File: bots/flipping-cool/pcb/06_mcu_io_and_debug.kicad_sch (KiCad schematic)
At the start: 12 parts, among them J12 UART_PROGRAM_HEADER, J13 USB_C_GCT_USB4085, J44 DEBUG_UART_TX_RX, J46 DEBUG_EN_BOOT, J47 DEBUG_MODE_SENSE, J48 DEBUG_ADC, J49 STEMMA_QT_I2C, U10 ESP32-S3-WROOM-1, U11 USBLC6-2SC6

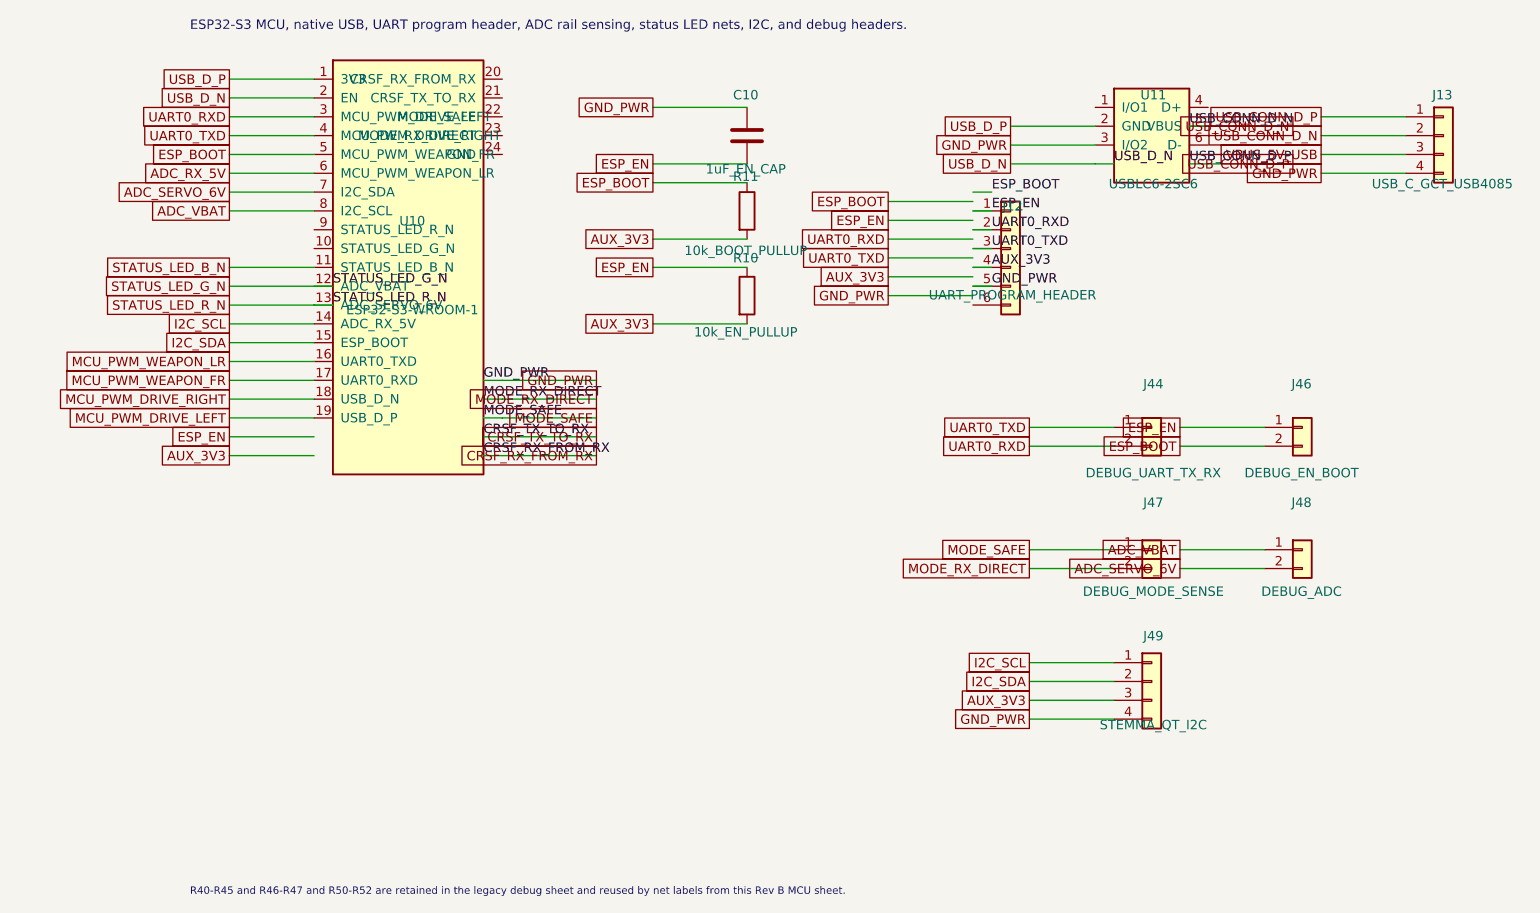
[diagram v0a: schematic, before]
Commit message: Remove obsolete Flipping Cool Rev B project plan file and update schematic files to reflect the latest design changes, including integration of the ESP32-S3 module and enhancements to power management and control authority. Ensure all documentation is aligned with the current PCB design and architecture.
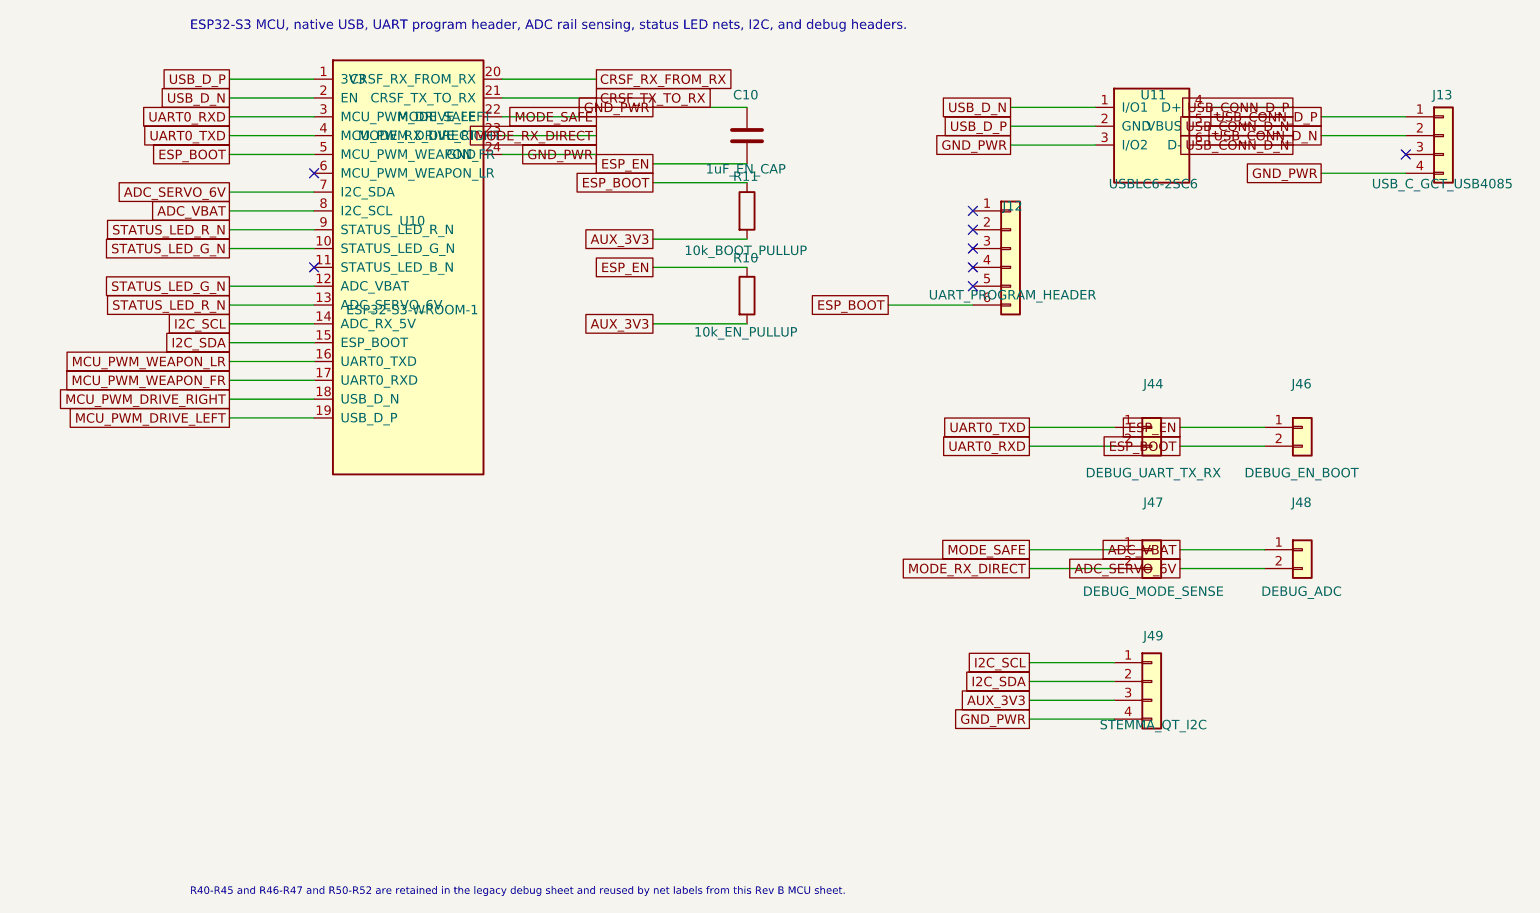
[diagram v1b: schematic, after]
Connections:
- net AUX_3V3: no longer J12.4 (Pin_4)
- net CRSF_RX_FROM_RX: now also U10.20 (CRSF_RX_FROM_RX)
- net CRSF_TX_TO_RX: now also U10.21 (CRSF_TX_TO_RX)
- net ESP_BOOT: now also J12.6 (Pin_6)
- net ESP_EN: no longer J12.1 (Pin_1)
- net GND_PWR: now also U10.24 (GND); no longer J12.5 (Pin_5)
- net MODE_RX_DIRECT: now also U10.23 (MODE_RX_DIRECT)
- net MODE_SAFE: now also U10.22 (MODE_SAFE)
- net STATUS_LED_G_N: now also U10.10 (STATUS_LED_G_N)
- net STATUS_LED_R_N: now also U10.9 (STATUS_LED_R_N)
- net UART0_RXD: no longer J12.2 (Pin_2)
- net UART0_TXD: no longer J12.3 (Pin_3)
- net USB_CONN_D_N: now also U11.6 (D-)
- net USB_CONN_D_P: now also U11.4 (D+)
- net USB_D_N: now also U11.1 (I/O1)
- net ADC_RX_5V: no longer names the net of U10.6 (MCU_PWM_WEAPON_LR)
- net STATUS_LED_B_N: no longer names the net of U10.11 (STATUS_LED_B_N)
- net VBUS_5V_USB: no longer names the net of J13.3 (Pin_3)
- no-connect marks 0 -> 8
